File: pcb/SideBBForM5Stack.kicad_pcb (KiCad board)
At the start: 2 copper layers, 100 x 50 mm, 15 parts, among them J1 Conn_01x15, J2 Conn_01x15, J3 Conn_02x15_Odd_Even, J4 Conn_02x15_Odd_Even

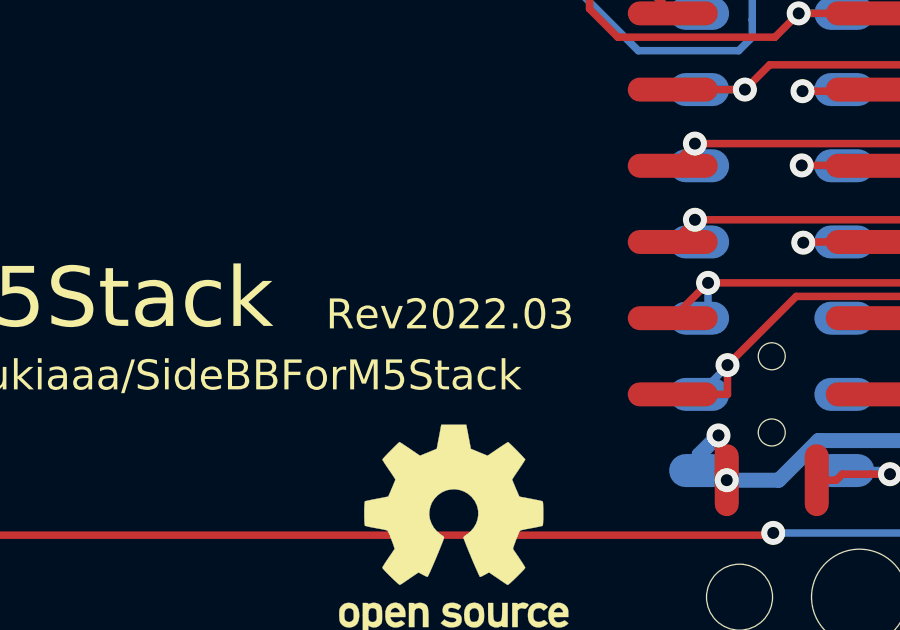
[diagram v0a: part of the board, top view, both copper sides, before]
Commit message: Update filling of main pcb
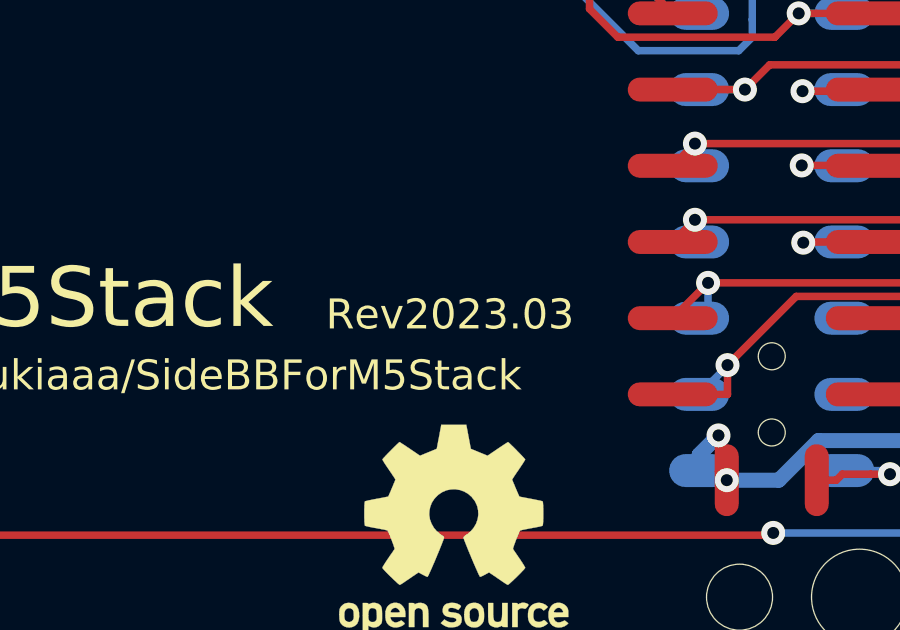
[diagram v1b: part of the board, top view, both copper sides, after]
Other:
- board text added: "Rev2023.03"
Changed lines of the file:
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@@
     (effects (font (size 1 1) (thickness 0.25)))
   )
-  (gr_text "Rev2022.03" (at 133.3488 87.5792) (layer "F.SilkS")
+  (gr_text "Rev2023.03" (at 133.3488 87.5792) (layer "F.SilkS")
     (effects (font (size 1 1) (thickness 0.25)))
   )

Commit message: Correct revision on back silks
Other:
- board text removed: "Rev2022.03"
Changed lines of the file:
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@@
     (effects (font (size 2.5 2.5) (thickness 0.625)) (justify mirror))
   )
-  (gr_text "Rev2022.03" (at 158.1988 87.8832) (layer "B.SilkS")
+  (gr_text "Rev2023.03" (at 158.1988 87.8832) (layer "B.SilkS")
     (effects (font (size 1.2 1.2) (thickness 0.3)) (justify mirror))
   )
